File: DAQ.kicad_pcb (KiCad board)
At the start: 2 copper layers, 99 x 99 mm, 142 parts, among them J1 ICD15S13E4GX00LF, J2 ICD15S13E4GX00LF, J3 ICD15S13E4GX00LF, P1 0022272021, U1 ADS124S08IRHBT, U2 ADS124S08IRHBT, U3 LT6654BMPS6-5-TRMPBF, U4 LM1086IS-5.0_NOPB, U5 TPS73801DCQR, U6 TPSM63603RDHR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

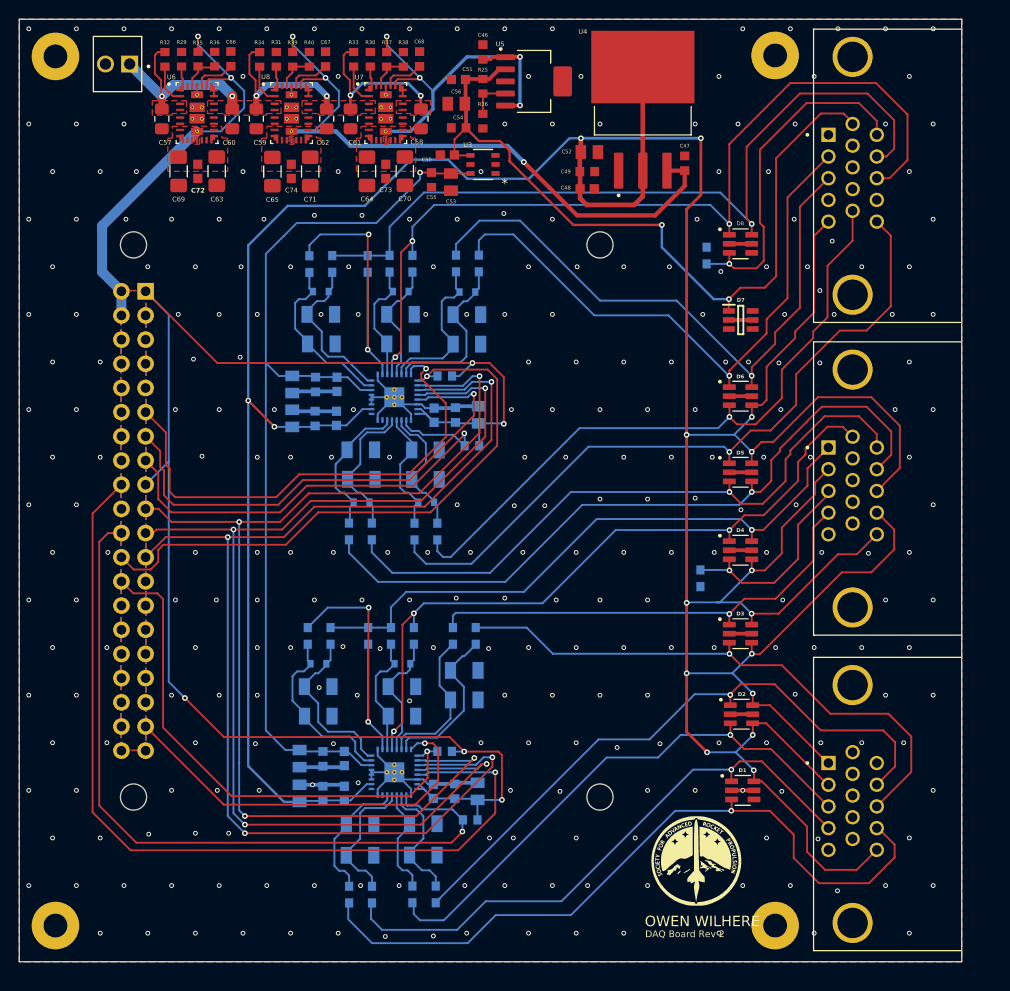
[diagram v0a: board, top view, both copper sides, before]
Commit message: Clean up schematic
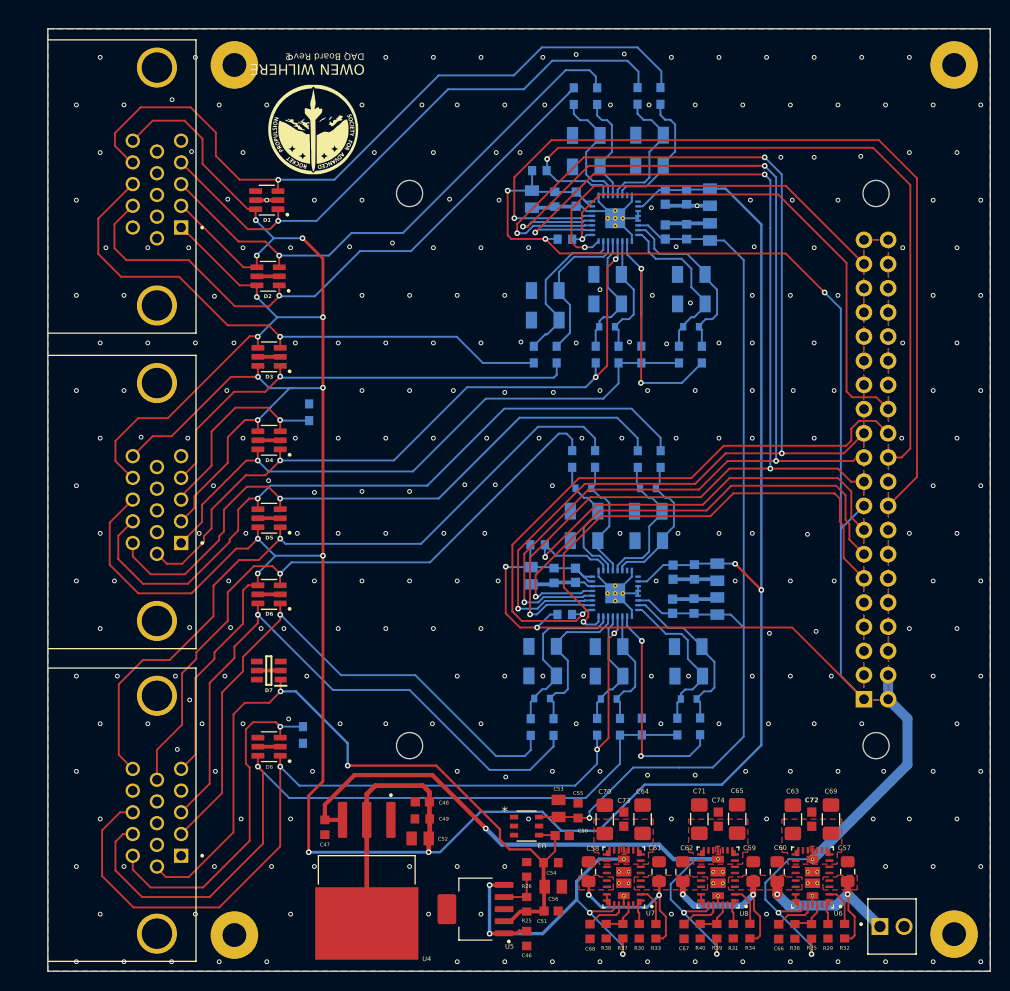
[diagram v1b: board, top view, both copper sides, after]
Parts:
- moved H2 132.0 mm to (178.2, 136.1), turned to 180 degrees
- moved H4 130.7 mm to (178.2, 44.8), turned to 180 degrees
- moved P1 121.8 mm to (171.7, 135.3), turned to 180 degrees
- moved R32 116.1 mm to (166.7, 135.8), turned to -90 degrees
- moved R29 114.0 mm to (164.9, 135.8), turned to 90 degrees
- moved R35 112.0 mm to (163.2, 135.8), turned to -90 degrees
- moved R36 110.0 mm to (161.5, 135.8), turned to 90 degrees
- moved H1 108.5 mm to (102.6, 136.2), turned to 180 degrees
- moved C66 108.2 mm to (159.8, 135.8), turned to -90 degrees
- moved C57 107.0 mm to (167.0, 129.5), turned to -90 degrees
- moved H3 106.8 mm to (102.6, 44.8), turned to 180 degrees
- moved R34 105.1 mm to (156.8, 135.8), turned to -90 degrees
- moved R31 103.4 mm to (155.0, 135.8), turned to 90 degrees
- moved U6 103.1 mm to (163.3, 130.2), turned to 180 degrees
- moved R39 101.9 mm to (153.3, 135.8), turned to -90 degrees
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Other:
- board text added: "Load Cell: TOP: power+ BOTTOM: power- LEFT: sig+ RIGHT: sig-"
- board text added: "PT: BOTTOM: sig LEFT: GND RIGHT: Power"
- board text added: "RTD: (based on ADC data sheet diagram) BOTTOM: L1 LEFT: L2 RIGHT: L3"
